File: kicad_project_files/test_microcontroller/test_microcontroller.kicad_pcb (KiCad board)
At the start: 2 copper layers, 60 x 100 mm, 40 parts, among them J1 USB_C_Receptacle_USB2.0, SW1 SW_Push, SW2 SW_Push, SW3 SW_Push, SW4 SW_Push, SW5 SW_Push, SW6 SW_Push, SW7 SW_Push, SW8 SW_Push, SW9 SW_Push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

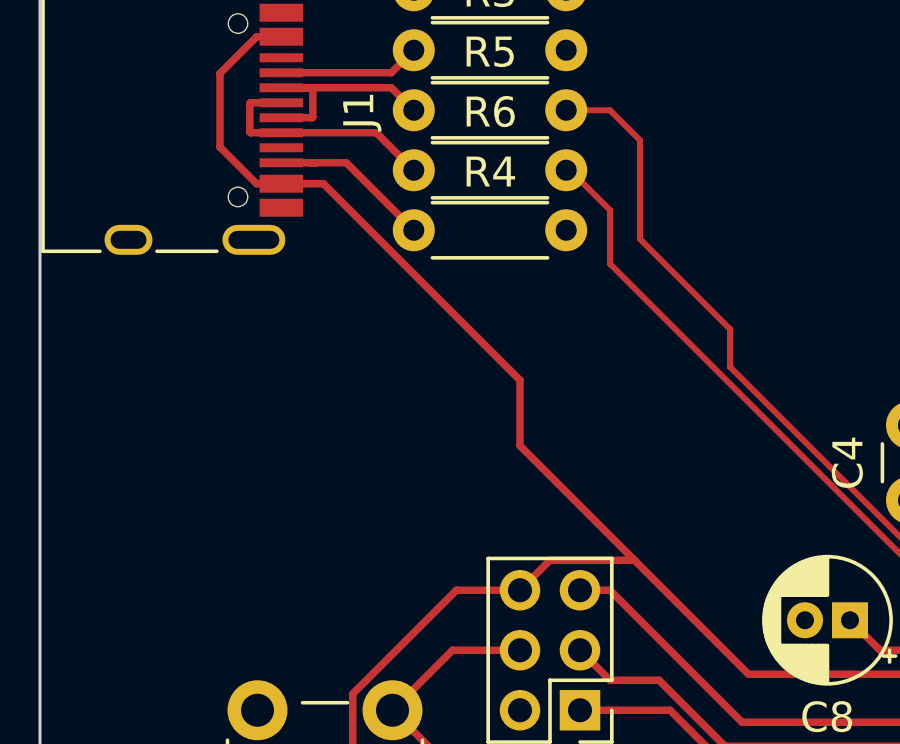
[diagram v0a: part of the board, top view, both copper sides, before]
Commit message: add diode to pcb
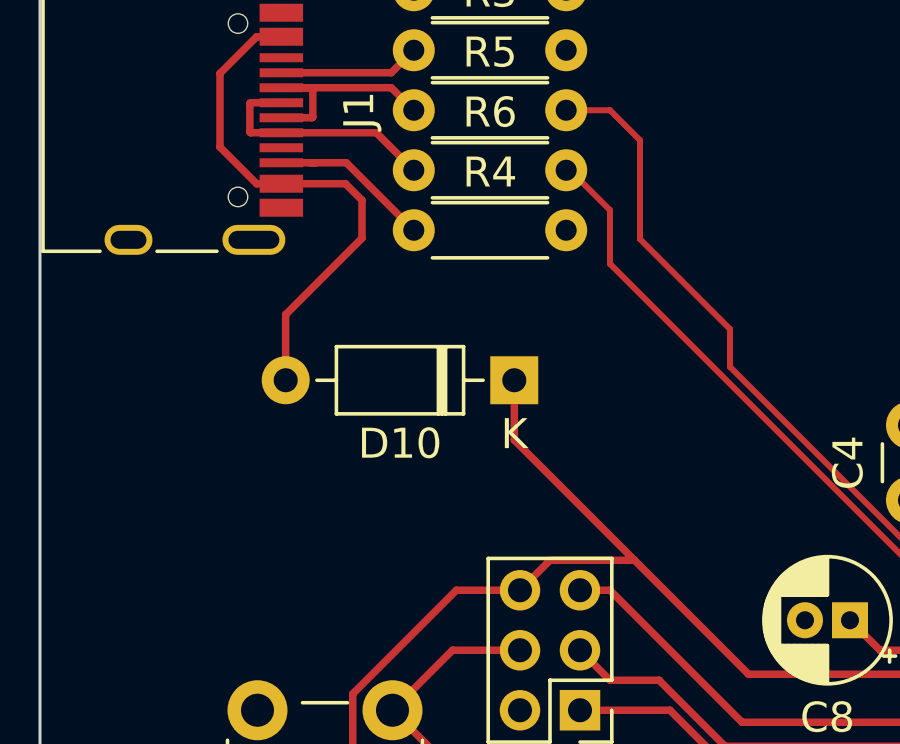
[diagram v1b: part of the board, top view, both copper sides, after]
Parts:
- added D10: 1N4148, Diode_THT:D_DO-35_SOD27_P7.62mm_Horizontal, F.Cu at (44.8, 36.0)
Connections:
- J1 pad A4: VCC -> Net-(J1-PadA4)
- J1 pad A9: VCC -> Net-(J1-PadA4)
- J1 pad B4: VCC -> Net-(J1-PadA4)
- J1 pad B9: VCC -> Net-(J1-PadA4)
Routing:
- net VCC: track 138.5 -> 120.4 mm
- net Net-(J1-PadA4): track 0.00 -> 17.5 mm
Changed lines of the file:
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@@
   (net 51 "unconnected-(U1-Pad42)")
   (net 52 "VCC")
+  (net 53 "Net-(J1-PadA4)")
   (footprint "Diode_THT:D_DO-35_SOD27_P7.62mm_Horizontal" (layer "F.Cu")
     (at 53 115.81 90)
@@
       (net 1 "GNDREF") (pinfunction "GND") (pintype "passive"))
     (pad "A4" smd rect (at -2.45 -4.045 270) (size 0.6 1.45) (layers "F.Cu" "F.Paste" "F.Mask")
-      (net 52 "VCC") (pinfunction "VBUS") (pintype "passive"))
+      (net 53 "Net-(J1-PadA4)") (pinfunction "VBUS") (pintype "passive"))
     (pad "A5" smd rect (at -1.25 -4.045 270) (size 0.3 1.45) (layers "F.Cu" "F.Paste" "F.Mask")
       (net 18 "Net-(J1-PadA5)") (pinfunction "CC1") (pintype "bidirectional"))
@@
       (net 21 "unconnected-(J1-PadA8)") (pinfunction "SBU1") (pintype "bidirectional+no_connect"))
     (pad "A9" smd rect (at 2.45 -4.045 270) (size 0.6 1.45) (layers "F.Cu" "F.Paste" "F.Mask")
-      (net 52 "VCC") (pinfunction "VBUS") (pintype "passive"))
+      (net 53 "Net-(J1-PadA4)") (pinfunction "VBUS") (pintype "passive"))
     (pad "A12" smd rect (at 3.25 -4.045 270) (size 0.6 1.45) (layers "F.Cu" "F.Paste" "F.Mask")
       (net 1 "GNDREF") (pinfunction "GND") (pintype "passive"))
@@
       (net 1 "GNDREF") (pinfunction "GND") (pintype "passive"))
     (pad "B4" smd rect (at 2.45 -4.045 270) (size 0.6 1.45) (layers "F.Cu" "F.Paste" "F.Mask")
-      (net 52 "VCC") (pinfunction "VBUS") (pintype "passive"))
+      (net 53 "Net-(J1-PadA4)") (pinfunction "VBUS") (pintype "passive"))
     (pad "B5" smd rect (at 1.75 -4.045 270) (size 0.3 1.45) (layers "F.Cu" "F.Paste" "F.Mask")
       (net 22 "Net-(J1-PadB5)") (pinfunction "CC2") (pintype "bidirectional"))
@@
       (net 23 "unconnected-(J1-PadB8)") (pinfunction "SBU2") (pintype "bidirectional+no_connect"))
     (pad "B9" smd rect (at -2.45 -4.045 270) (size 0.6 1.45) (layers "F.Cu" "F.Paste" "F.Mask")
-      (net 52 "VCC") (pinfunction "VBUS") (pintype "passive"))
+      (net 53 "Net-(J1-PadA4)") (pinfunction "VBUS") (pintype "passive"))
     (pad "B12" smd rect (at -3.25 -4.045 270) (size 0.6 1.45) (layers "F.Cu" "F.Paste" "F.Mask")
       (net 1 "GNDREF") (pinfunction "GND") (pintype "passive"))
@@
       (net 1 "GNDREF") (pintype "passive"))
     (model "${KICAD6_3DMODEL_DIR}/Capacitor_THT.3dshapes/CP_Radial_D4.0mm_P1.50mm.wrl"
+      (offset (xyz 0 0 0))
+      (scale (xyz 1 1 1))
+      (rotate (xyz 0 0 0))
+    )
+  )
+  (footprint "Diode_THT:D_DO-35_SOD27_P7.62mm_Horizontal" (layer "F.Cu")
+    (at 44.81 36 180)
+    (descr "Diode, DO-35_SOD27 series, Axial, Horizontal, pin pitch=7.62mm, , length*diameter=4*2mm^2, , http://www.diodes.com/_files/packages/DO-35.pdf")
+    (tags "Diode DO-35_SOD27 series Axial Horizontal pin pitch 7.62mm  length 4mm diameter 2mm")
+    (property "Sheetfile" "test_microcontroller.kicad_sch")
+    (property "Sheetname" "")
+    (attr through_hole)
+    (fp_text reference "D10" (at 3.81 -2.12) (layer "F.SilkS")
+      (effects (font (size 1 1) (thickness 0.15)))
+    )
+    (fp_text value "1N4148" (at 3.81 2.12) (layer "F.Fab")
+      (effects (font (size 1 1) (thickness 0.15)))
+    )
+    (fp_text user "K" (at 0 -1.8) (layer "F.SilkS")
+      (effects (font (size 1 1) (thickness 0.15)))
+    )
+    (fp_text user "K" (at 0 -1.8) (layer "F.Fab")
+      (effects (font (size 1 1) (thickness 0.15)))
+    )
+    (fp_text user "${REFERENCE}" (at 4.11 0) (layer "F.Fab")
+      (effects (font (size 0.8 0.8) (thickness 0.12)))
+    )
+    (fp_line (start 5.93 -1.12) (end 1.69 -1.12) (layer "F.SilkS") (width 0.12))
+    (fp_line (start 5.93 1.12) (end 5.93 -1.12) (layer "F.SilkS") (width 0.12))
+    (fp_line (start 1.69 1.12) (end 5.93 1.12) (layer "F.SilkS") (width 0.12))
+    (fp_line (start 1.04 0) (end 1.69 0) (layer "F.SilkS") (width 0.12))
+    (fp_line (start 2.41 -1.12) (end 2.41 1.12) (layer "F.SilkS") (width 0.12))
+    (fp_line (start 2.29 -1.12) (end 2.29 1.12) (layer "F.SilkS") (width 0.12))
+    (fp_line (start 1.69 -1.12) (end 1.69 1.12) (layer "F.SilkS") (width 0.12))
+    (fp_line (start 2.53 -1.12) (end 2.53 1.12) (layer "F.SilkS") (width 0.12))
+    (fp_line (start 6.58 0) (end 5.93 0) (layer "F.SilkS") (width 0.12))
+    (fp_line (start -1.05 1.25) (end 8.67 1.25) (layer "F.CrtYd") (width 0.05))
+    (fp_line (start 8.67 -1.25) (end -1.05 -1.25) (layer "F.CrtYd") (width 0.05))
+    (fp_line (start 8.67 1.25) (end 8.67 -1.25) (layer "F.CrtYd") (width 0.05))
+    (fp_line (start -1.05 -1.25) (end -1.05 1.25) (layer "F.CrtYd") (width 0.05))
+    (fp_line (start 5.81 1) (end 5.81 -1) (layer "F.Fab") (width 0.1))
+    (fp_line (start 2.51 -1) (end 2.51 1) (layer "F.Fab") (width 0.1))
+    (fp_line (start 5.81 -1) (end 1.81 -1) (layer "F.Fab") (width 0.1))
+    (fp_line (start 1.81 1) (end 5.81 1) (layer "F.Fab") (width 0.1))
+    (fp_line (start 2.31 -1) (end 2.31 1) (layer "F.Fab") (width 0.1))
+    (fp_line (start 7.62 0) (end 5.81 0) (layer "F.Fab") (width 0.1))
+    (fp_line (start 2.41 -1) (end 2.41 1) (layer "F.Fab") (width 0.1))
+    (fp_line (start 0 0) (end 1.81 0) (layer "F.Fab") (width 0.1))
+    (fp_line (start 1.81 -1) (end 1.81 1) (layer "F.Fab") (width 0.1))
+    (pad "1" thru_hole rect (at 0 0 180) (size 1.6 1.6) (drill 0.8) (layers *.Cu *.Mask)
+      (net 52 "VCC") (pinfunction "K") (pintype "passive"))
+    (pad "2" thru_hole oval (at 7.62 0 180) (size 1.6 1.6) (drill 0.8) (layers *.Cu *.Mask)
+      (net 53 "Net-(J1-PadA4)") (pinfunction "A") (pintype "passive"))
+    (model "${KICAD6_3DMODEL_DIR}/Diode_THT.3dshapes/D_DO-35_SOD27_P7.62mm_Horizontal.wrl"
       (offset (xyz 0 0 0))
       (scale (xyz 1 1 1))
@@
   (segment (start 61.3 48.2) (end 51.835718 48.2) (width 0.25) (layer "F.Cu") (net 36))
   (segment (start 64.6 50.7) (end 64.6 47.4) (width 0.25) (layer "F.Cu") (net 52))
-  (segment (start 45 38.182141) (end 45 36) (width 0.25) (layer "F.Cu") (net 52))
-  (segment (start 37.045 29.45) (end 36.220978 29.45) (width 0.25) (layer "F.Cu") (net 52))
-  (segment (start 48.818348 42.000489) (end 45 38.182141) (width 0.25) (layer "F.Cu") (net 52))
+  (segment (start 44.81 37.992141) (end 44.81 36) (width 0.25) (layer "F.Cu") (net 52))
   (segment (start 61.3 41.8) (end 59.8 41.8) (width 0.25) (layer "F.Cu") (net 52))
-  (segment (start 45 36) (end 38.45 29.45) (width 0.25) (layer "F.Cu") (net 52))
   (segment (start 39.425489 48.425489) (end 46.54 55.54) (width 0.25) (layer "F.Cu") (net 52))
   (segment (start 67 44.3) (end 70.925489 40.374511) (width 0.25) (layer "F.Cu") (net 52))
@@
   (segment (start 70.2 48.2) (end 67 45) (width 0.25) (layer "F.Cu") (net 52))
   (segment (start 71 40.3) (end 70.925489 40.374511) (width 0.25) (layer "F.Cu") (net 52))
-  (segment (start 36.220978 24.55) (end 37.045 24.55) (width 0.25) (layer "F.Cu") (net 52))
   (segment (start 77 50) (end 75.2 48.2) (width 0.25) (layer "F.Cu") (net 52))
   (segment (start 67 45) (end 67 44.3) (width 0.25) (layer "F.Cu") (net 52))
   (segment (start 62.3 41.8) (end 63.374511 40.725489) (width 0.25) (layer "F.Cu") (net 52))
+  (segment (start 48.818348 42.000489) (end 44.81 37.992141) (width 0.25) (layer "F.Cu") (net 52))
   (segment (start 64.6 51.7) (end 62.3 54) (width 0.25) (layer "F.Cu") (net 52))
   (segment (start 71 39.3) (end 71 40.3) (width 0.25) (layer "F.Cu") (net 52))
   (segment (start 62 35) (end 62 38.3) (width 0.25) (layer "F.Cu") (net 52))
   (segment (start 39.425489 46.451368) (end 39.425489 48.425489) (width 0.25) (layer "F.Cu") (net 52))
-  (segment (start 35 28.229022) (end 35 25.770978) (width 0.25) (layer "F.Cu") (net 52))
   (segment (start 42.876857 43) (end 39.425489 46.451368) (width 0.25) (layer "F.Cu") (net 52))
   (segment (start 62 38.3) (end 63 39.3) (width 0.25) (layer "F.Cu") (net 52))
@@
   (segment (start 64.6 50.7) (end 64.6 51.7) (width 0.25) (layer "F.Cu") (net 52))
   (segment (start 46.54 55.54) (end 46.54 59) (width 0.25) (layer "F.Cu") (net 52))
-  (segment (start 35 25.770978) (end 36.220978 24.55) (width 0.25) (layer "F.Cu") (net 52))
   (segment (start 62.3 54) (end 59 54) (width 0.25) (layer "F.Cu") (net 52))
   (segment (start 61.3 41.8) (end 62.3 41.8) (width 0.25) (layer "F.Cu") (net 52))
@@
   (segment (start 64.6 47.4) (end 67 45) (width 0.25) (layer "F.Cu") (net 52))
   (segment (start 72 35) (end 72 38.3) (width 0.25) (layer "F.Cu") (net 52))
-  (segment (start 38.45 29.45) (end 37.045 29.45) (width 0.25) (layer "F.Cu") (net 52))
   (segment (start 45 43) (end 42.876857 43) (width 0.25) (layer "F.Cu") (net 52))
-  (segment (start 36.220978 29.45) (end 35 28.229022) (width 0.25) (layer "F.Cu") (net 52))
   (segment (start 72.7 48.2) (end 70.2 48.2) (width 0.25) (layer "F.Cu") (net 52))
+  (segment (start 37.045 29.45) (end 36.220978 29.45) (width 0.25) (layer "F.Cu") (net 53))
+  (segment (start 39.734511 30) (end 39.184511 29.45) (width 0.25) (layer "F.Cu") (net 53))
+  (segment (start 39.734511 31.265489) (end 39.734511 30) (width 0.25) (layer "F.Cu") (net 53))
+  (segment (start 36.220978 24.55) (end 37.045 24.55) (width 0.25) (layer "F.Cu") (net 53))
+  (segment (start 35 28.229022) (end 35 25.770978) (width 0.25) (layer "F.Cu") (net 53))
+  (segment (start 37.19 33.81) (end 39.734511 31.265489) (width 0.25) (layer "F.Cu") (net 53))
+  (segment (start 39.184511 29.45) (end 37.045 29.45) (width 0.25) (layer "F.Cu") (net 53))
+  (segment (start 35 25.770978) (end 36.220978 24.55) (width 0.25) (layer "F.Cu") (net 53))
+  (segment (start 37.19 36) (end 37.19 33.81) (width 0.25) (layer "F.Cu") (net 53))
+  (segment (start 36.220978 29.45) (end 35 28.229022) (width 0.25) (layer "F.Cu") (net 53))
   (zone (net 1) (net_name "GNDREF") (layer "F.Cu") (hatch edge 0.508)
     (connect_pads (clearance 0.3))
